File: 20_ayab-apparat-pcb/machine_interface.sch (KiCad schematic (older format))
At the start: 9 parts

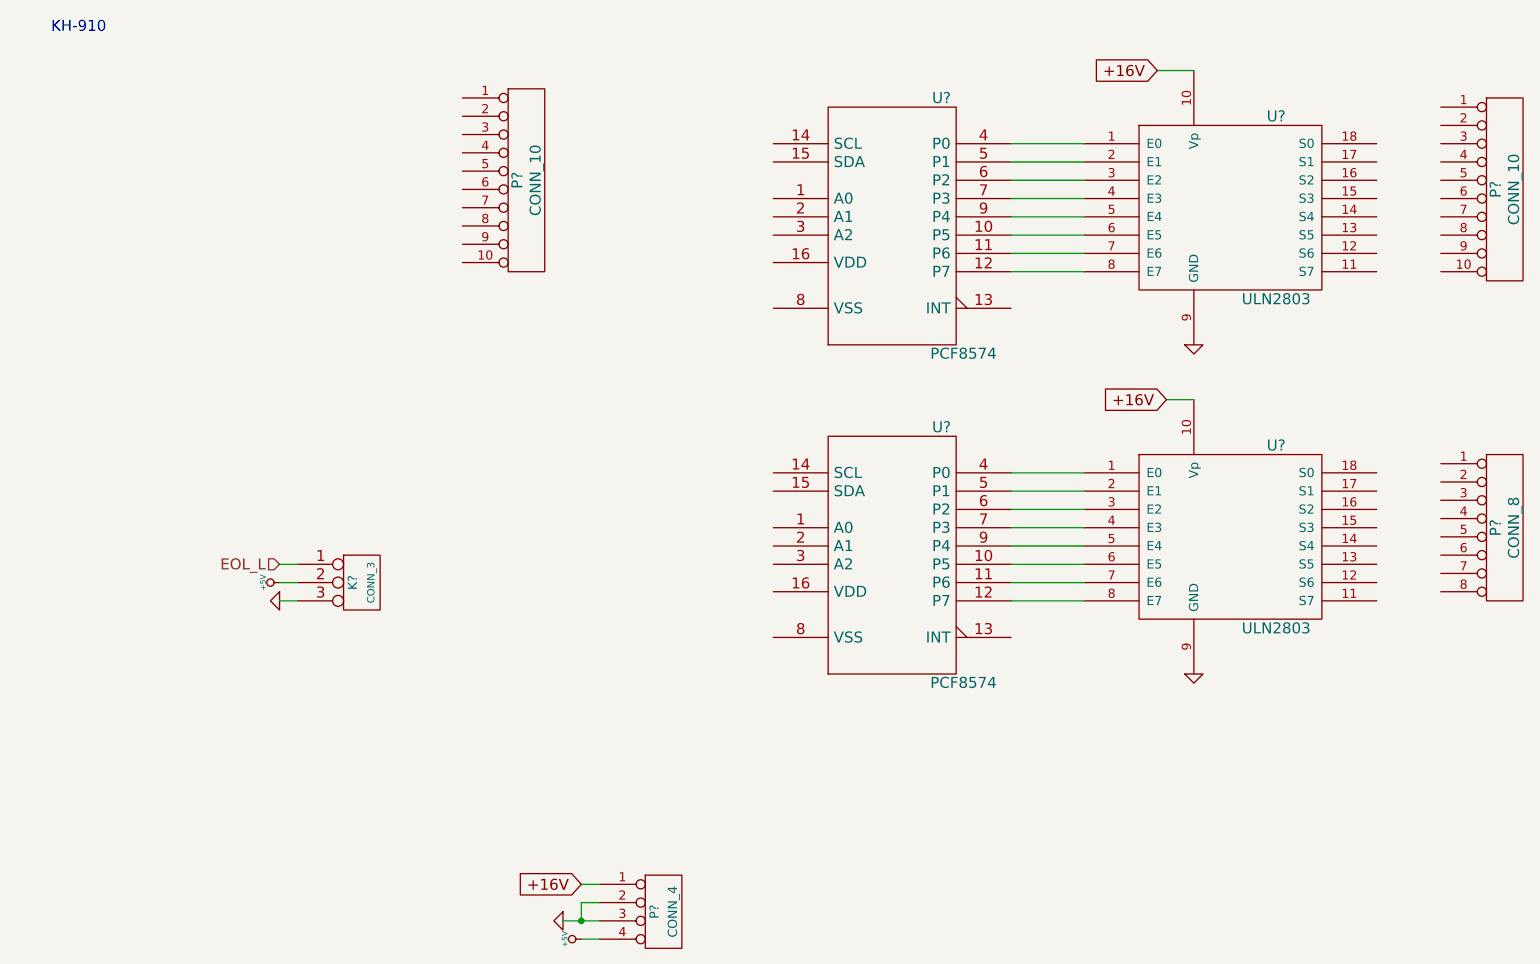
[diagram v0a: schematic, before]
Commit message: finished connectors for kh-910
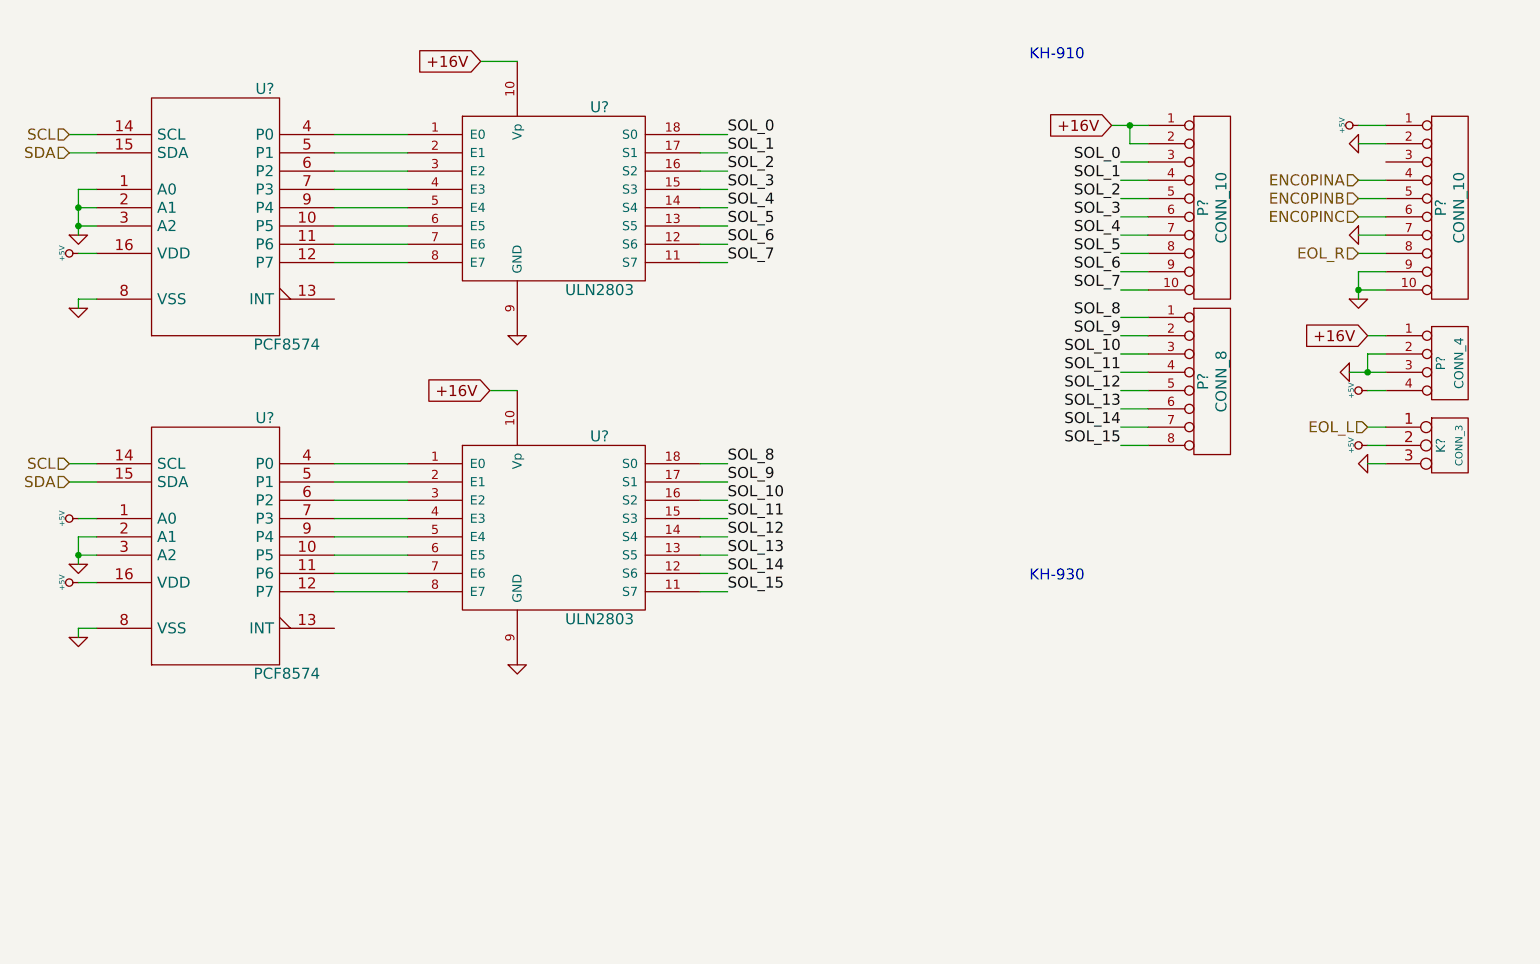
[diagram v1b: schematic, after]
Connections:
- net +16V: now also P?.1 (P1), P?.2 (P2)
- net +5V: now also P?.1 (P1), U?.1 (A0), U?.16 (VDD), U?.16 (VDD)
- net GND: now also P?.10 (P10), P?.2 (P2), P?.7 (P7), P?.9 (P9), U?.1 (A0), U?.2 (A1), U?.2 (A1), U?.3 (A2), U?.3 (A2), U?.8 (VSS), U?.8 (VSS)
- net SOL_7: now reaches P?.10 (P10)
- net SOL_7: now also U?.11 (S7)
- net SOL_0: now reaches P?.3 (P3)
- net SOL_0: now also U?.18 (S0)
- net SOL_1: now reaches P?.4 (P4)
- net SOL_1: now also U?.17 (S1)
- net SOL_2: now reaches P?.5 (P5)
- net SOL_2: now also U?.16 (S2)
- net SOL_3: now reaches P?.6 (P6)
- net SOL_3: now also U?.15 (S3)
- net SOL_4: now reaches P?.7 (P7)
- net SOL_4: now also U?.14 (S4)
- net SOL_5: now reaches P?.8 (P8)
- net SOL_5: now also U?.13 (S5)
- net SOL_6: now reaches P?.9 (P9)
- net SOL_6: now also U?.12 (S6)
- net SOL_8: now reaches P?.1 (P1)
- net SOL_8: now also U?.18 (S0)
- net SOL_9: now reaches P?.2 (P2)
- net SOL_9: now also U?.17 (S1)
- net SOL_10: now reaches P?.3 (P3)
- net SOL_10: now also U?.16 (S2)
- net SOL_11: now reaches P?.4 (P4)
- net SOL_11: now also U?.15 (S3)
- net SOL_12: now reaches P?.5 (P5)
- net SOL_12: now also U?.14 (S4)
- net SOL_13: now reaches P?.6 (P6)
- net SOL_13: now also U?.13 (S5)
- net SOL_14: now reaches P?.7 (P7)
- net SOL_14: now also U?.12 (S6)
- net SOL_15: now reaches P?.8 (P8)
- net SOL_15: now also U?.11 (S7)
- net ENC0PINA: now reaches P?.4 (P4)
- net ENC0PINB: now reaches P?.5 (P5)
- net ENC0PINC: now reaches P?.6 (P6)
- net EOL_R: now reaches P?.8 (P8)
- net SCL: now reaches U?.14 (SCL)
- net SCL: now also U?.14 (SCL)
- net SDA: now reaches U?.15 (SDA)
- net SDA: now also U?.15 (SDA)
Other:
- note added: "KH-930"
- moved on the sheet: K?, P?, U?

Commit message: added atmega schematic
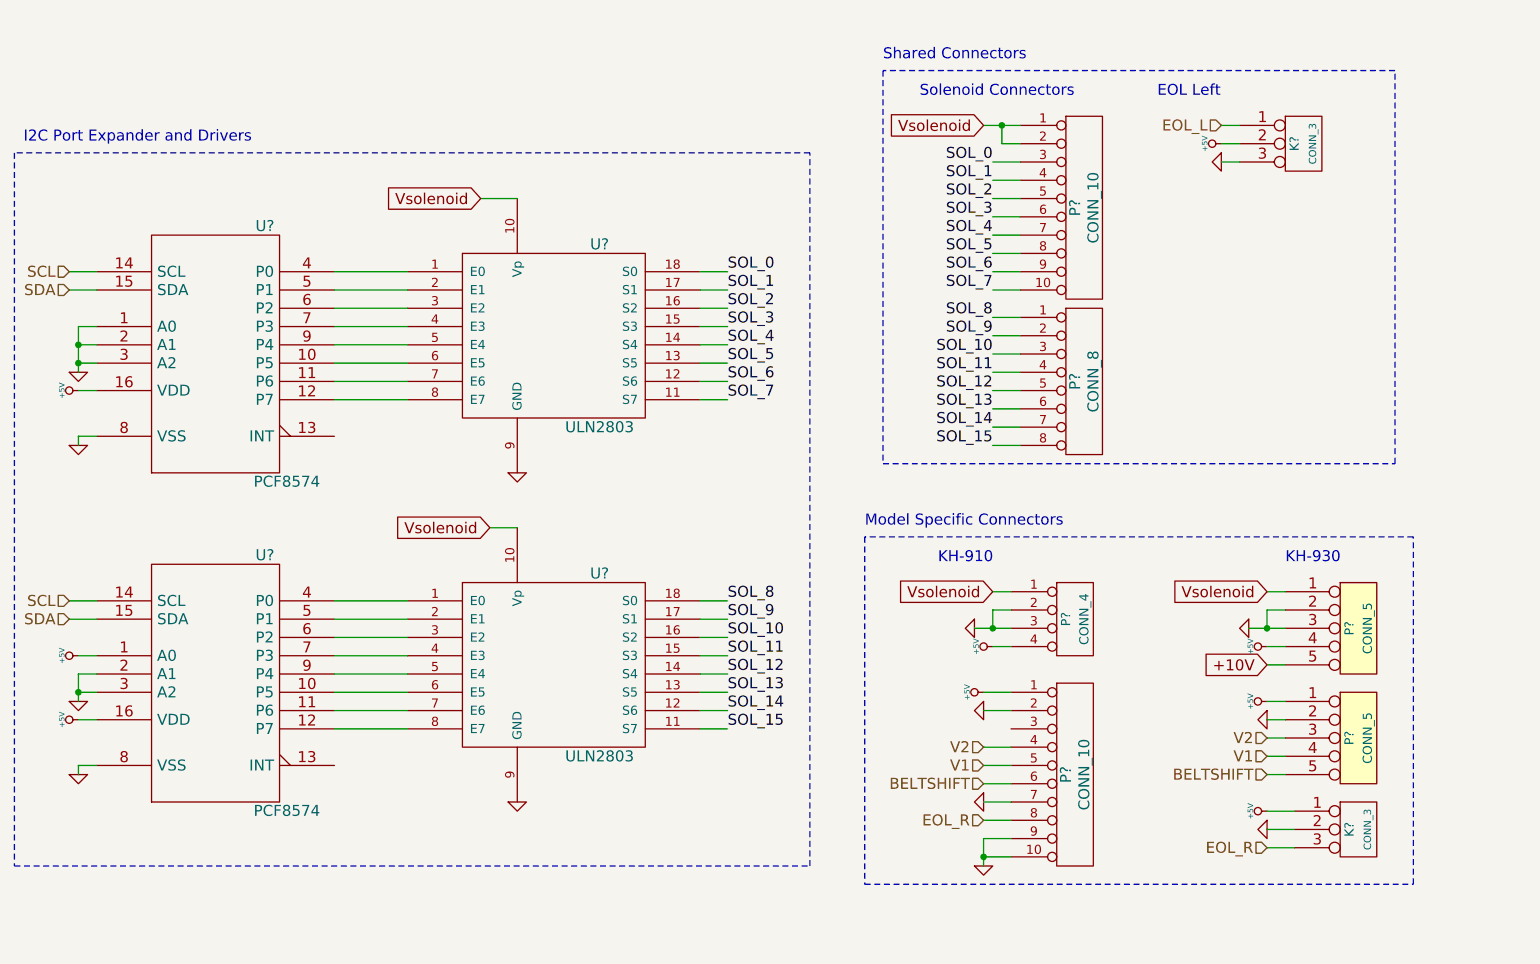
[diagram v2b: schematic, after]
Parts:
- added K?: CONN_3, symbol CONN_3
- added P? (x2): CONN_5, symbol CONN_5
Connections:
- net +5V: now also K?.1 (P1), P?.1, P?.4
- net EOL_R: now also K?.3 (P3)
- net GND: now also K?.2 (PM), P?.2, P?.2, P?.3
- net +16V renamed Vsolenoid
- net Vsolenoid: now also P?.1
- net ENC0PINA renamed V2
- net V2: now also P?.3
- net ENC0PINB renamed V1
- net V1: now also P?.4
- net ENC0PINC renamed BELTSHIFT
- net BELTSHIFT: now also P?.5
- new net +10V: P?.5
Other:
- note added: "EOL Left"
- note added: "I2C Port Expander and Drivers"
- note added: "Model Specific Connectors"
- note added: "Shared Connectors"
- note added: "Solenoid Connectors"
- moved on the sheet: K?, P?, U?

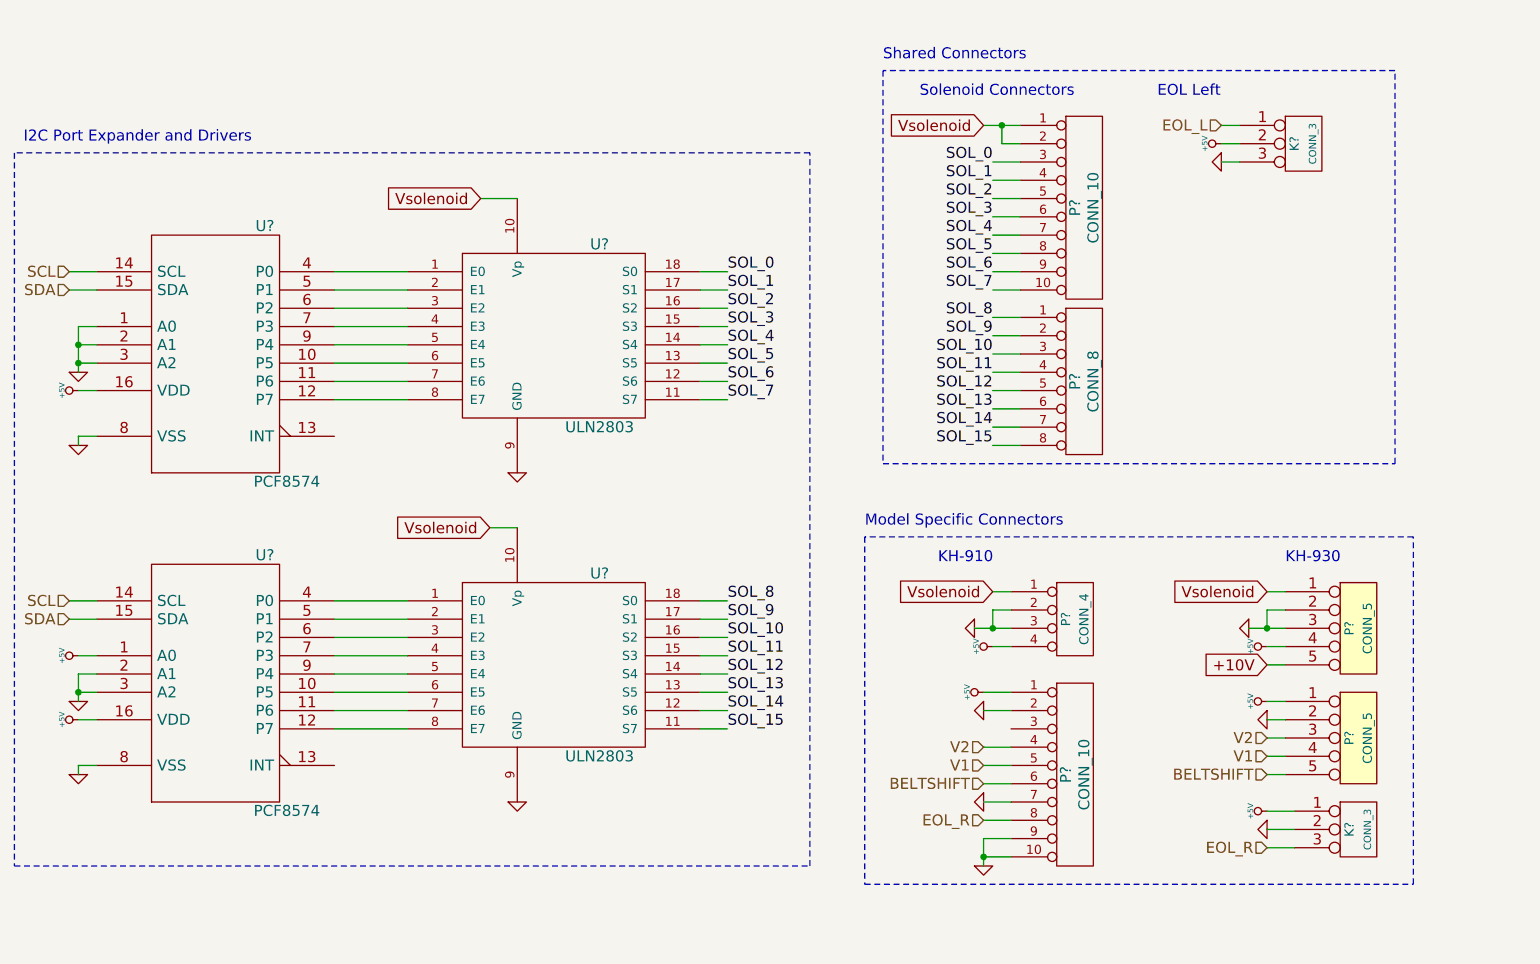
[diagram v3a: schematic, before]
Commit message: schematic structure finished -> todo add part values
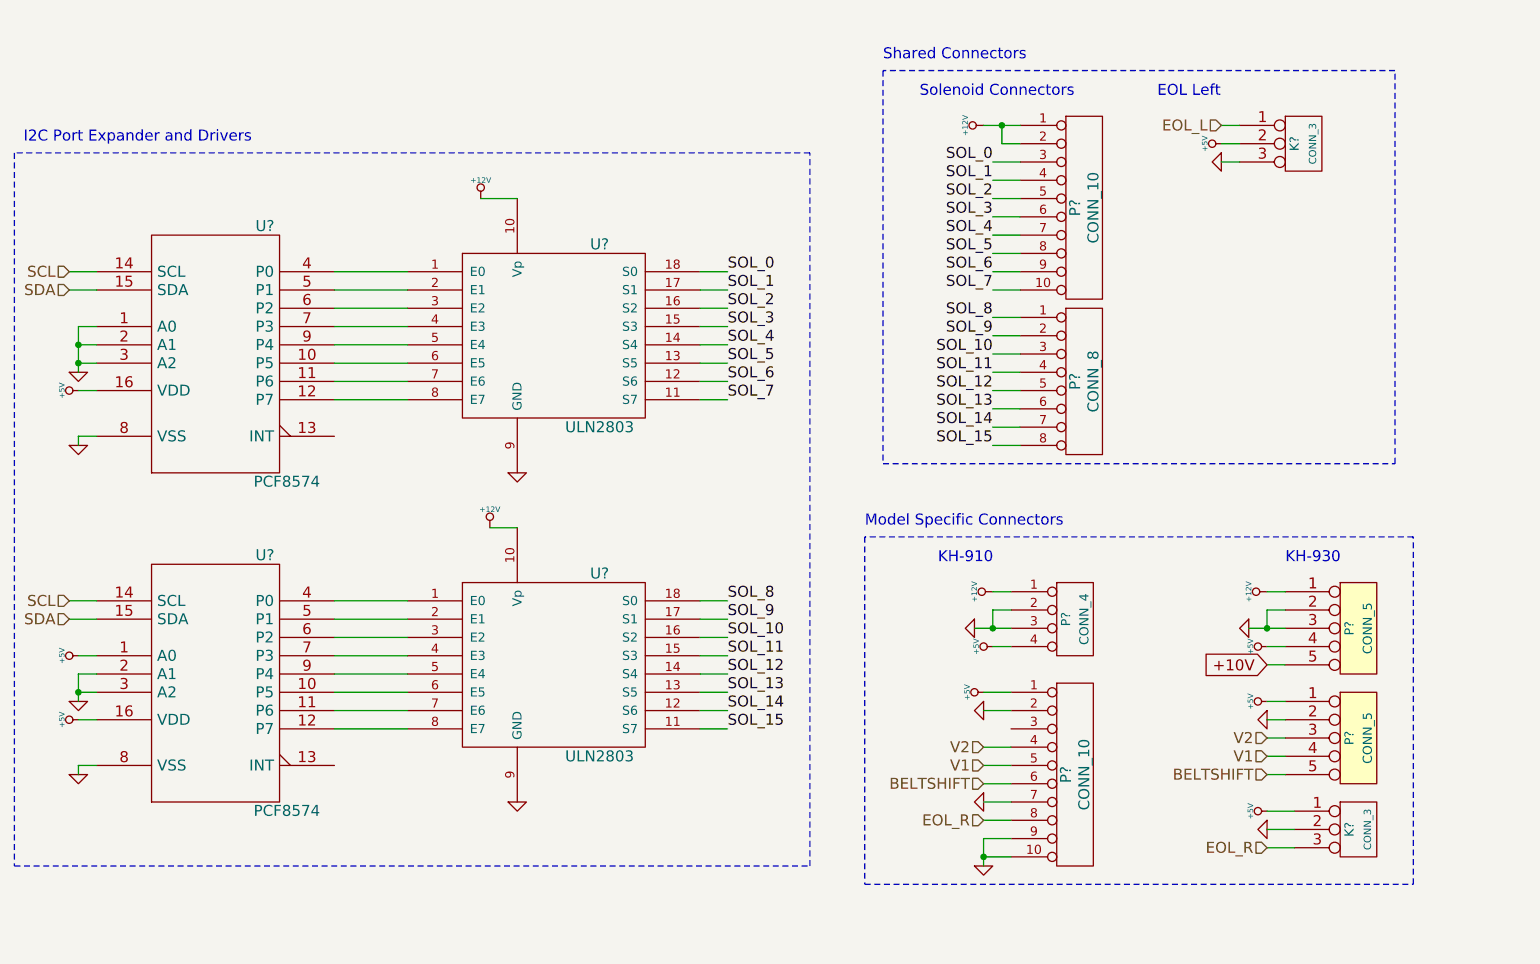
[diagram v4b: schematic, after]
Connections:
- net Vsolenoid renamed +12V
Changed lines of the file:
@@
 	0    -1   -1   0
 $EndComp
-Text GLabel 6400 4000 0    60   Input ~ 0
-Vsolenoid
 Text Notes 6100 3850 0    60   ~ 0
 KH-910
@@
 	1    0    0    -1
 $EndComp
-Text GLabel 3600 1850 0    60   Input ~ 0
-Vsolenoid
-Text GLabel 3650 3650 0    60   Input ~ 0
-Vsolenoid
-Text GLabel 6350 1450 0    60   Input ~ 0
-Vsolenoid
 $Comp
 L GND #PWR?
@@
 Wire Wire Line
 	7900 4300 8000 4300
-Text GLabel 7900 4000 0    60   Input ~ 0
-Vsolenoid
 Wire Wire Line
 	7900 4000 8000 4000
@@
 Wire Notes Line
 	8600 1150 5800 1150
+$Comp
+L +12V #PWR?
+U 1 1 52EA8D08
+P 6400 4000
+F 0 "#PWR?" H 6400 3950 20  0001 C CNN
+F 1 "+12V" H 6400 4100 30  0000 C CNN
+F 2 "" H 6400 4000 60  0000 C CNN
+F 3 "" H 6400 4000 60  0000 C CNN
+	1    6400 4000
+	0    -1   -1   0
+$EndComp
+$Comp
+L +12V #PWR?
+U 1 1 52EA8D1C
+P 7900 4000
+F 0 "#PWR?" H 7900 3950 20  0001 C CNN
+F 1 "+12V" H 7900 4100 30  0000 C CNN
+F 2 "" H 7900 4000 60  0000 C CNN
+F 3 "" H 7900 4000 60  0000 C CNN
+	1    7900 4000
+	0    -1   -1   0
+$EndComp
+$Comp
+L +12V #PWR?
+U 1 1 52EA8D30
+P 6350 1450
+F 0 "#PWR?" H 6350 1400 20  0001 C CNN
+F 1 "+12V" H 6350 1550 30  0000 C CNN
+F 2 "" H 6350 1450 60  0000 C CNN
+F 3 "" H 6350 1450 60  0000 C CNN
+	1    6350 1450
+	0    -1   -1   0
+$EndComp
+$Comp
+L +12V #PWR?
+U 1 1 52EA8D44
+P 3600 1850
+F 0 "#PWR?" H 3600 1800 20  0001 C CNN
+F 1 "+12V" H 3600 1950 30  0000 C CNN
+F 2 "" H 3600 1850 60  0000 C CNN
+F 3 "" H 3600 1850 60  0000 C CNN
+	1    3600 1850
+	1    0    0    -1
+$EndComp
+$Comp
+L +12V #PWR?
+U 1 1 52EA8D58
+P 3650 3650
+F 0 "#PWR?" H 3650 3600 20  0001 C CNN
+F 1 "+12V" H 3650 3750 30  0000 C CNN
+F 2 "" H 3650 3650 60  0000 C CNN
+F 3 "" H 3650 3650 60  0000 C CNN
+	1    3650 3650
+	1    0    0    -1
+$EndComp
 $EndSCHEMATC
